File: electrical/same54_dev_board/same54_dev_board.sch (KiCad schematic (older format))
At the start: 8 parts

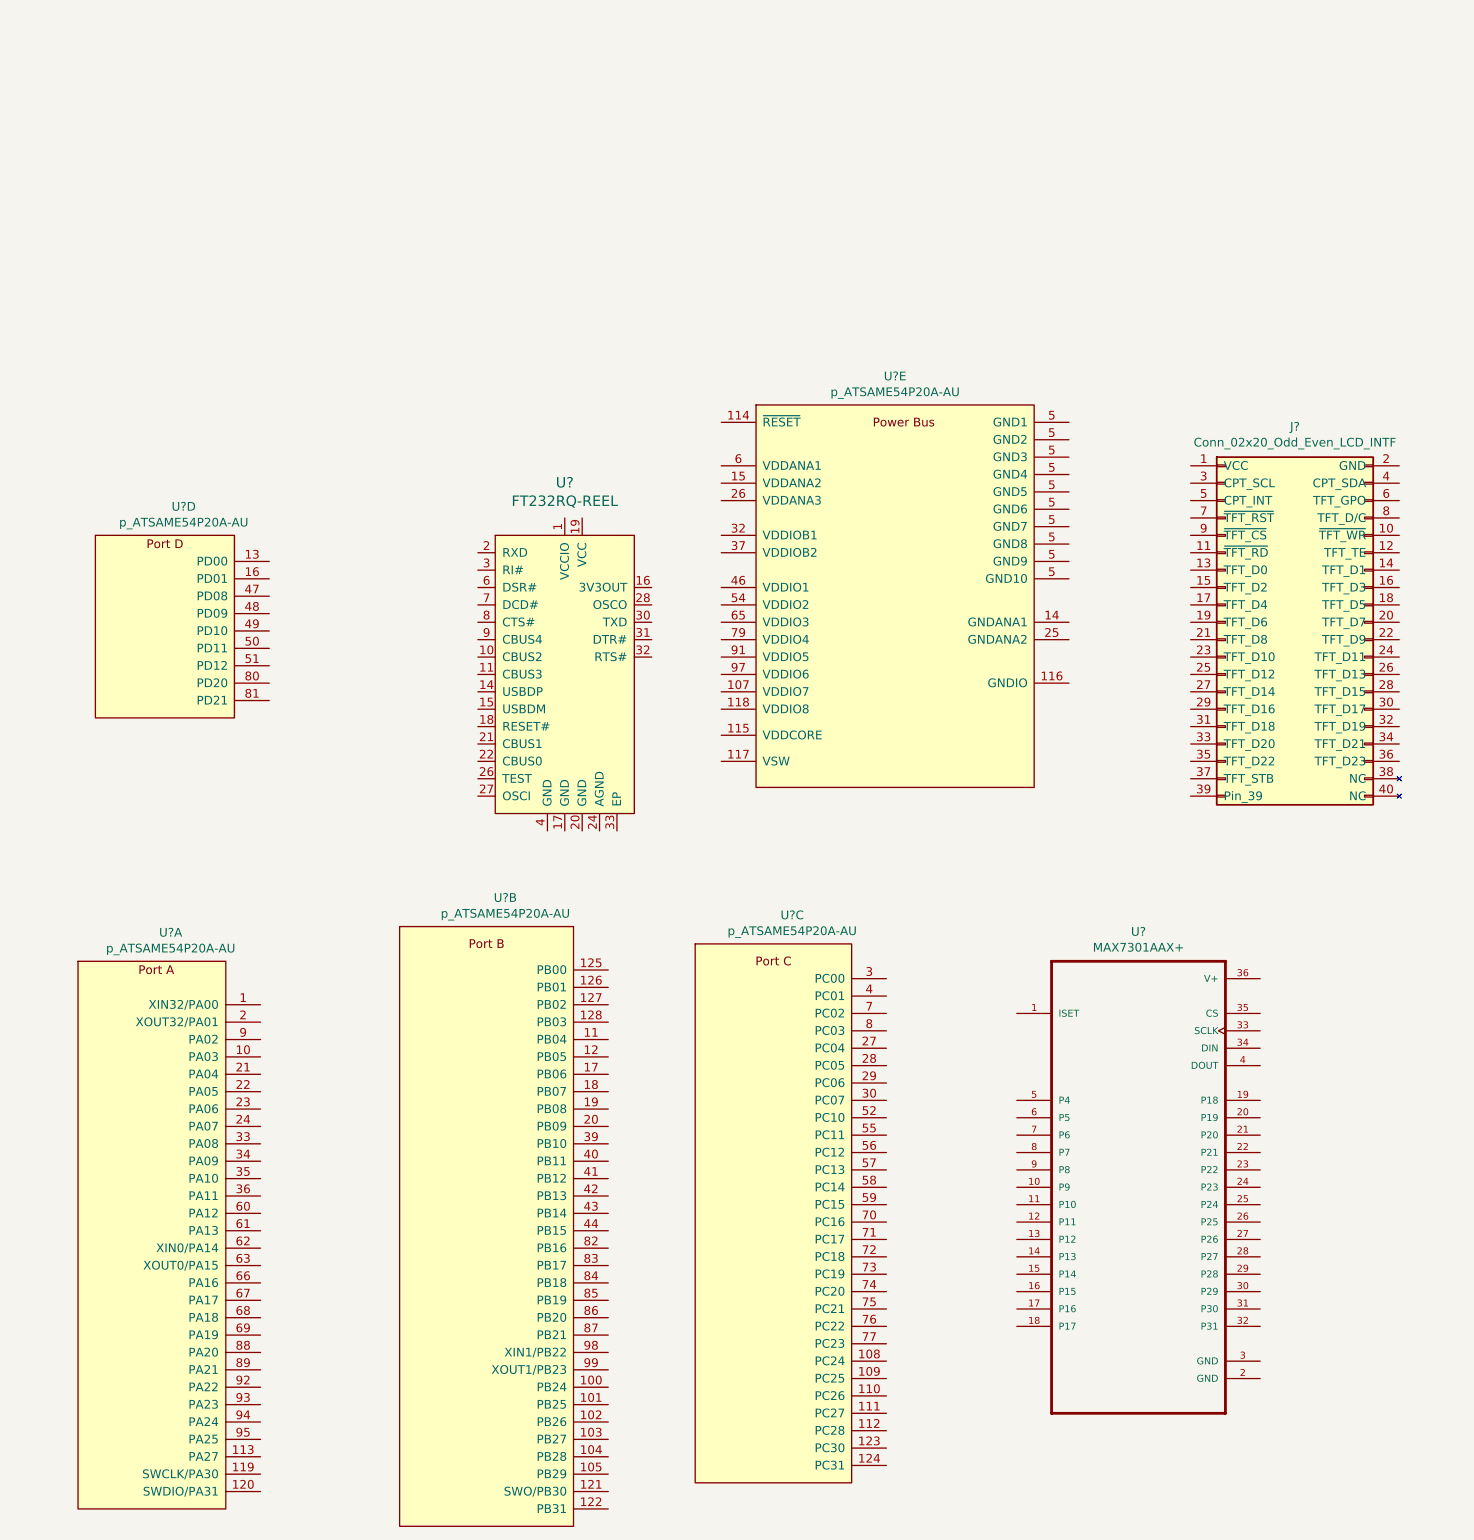
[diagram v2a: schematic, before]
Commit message: Added hierarchical pins for some components, finished io expander to lcd bus, going with 2x20 icd block header for the tft bus but dont have a part number for digikey
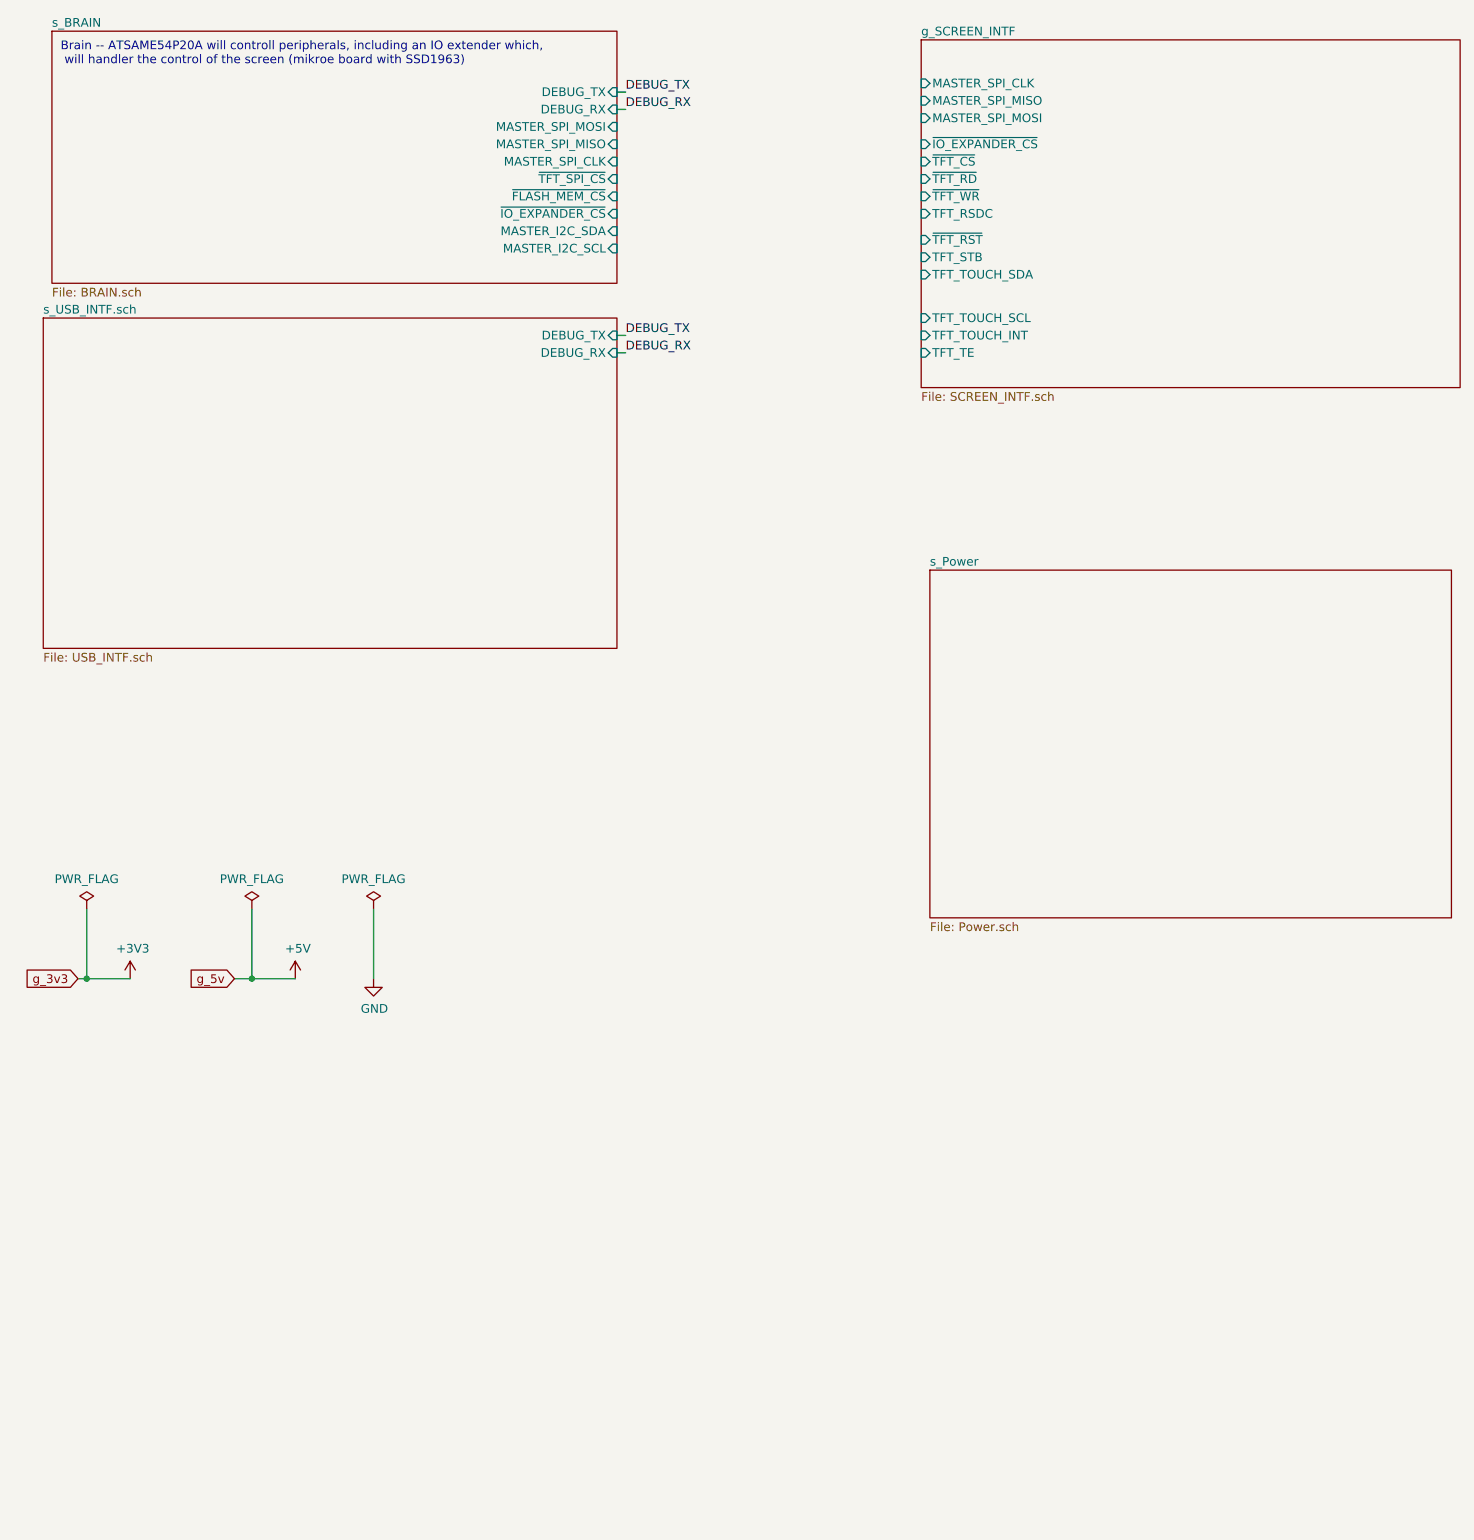
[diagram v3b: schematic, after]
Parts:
- removed J?: Conn_02x20_Odd_Even_LCD_INTF, symbol Conn_02x20_LCD_INTF:Conn_02x20_Odd_Even_LCD_INTF
- removed U?: FT232RQ-REEL, digikey-footprints:QFN-32-1EP_5x5mm, symbol dk_Interface-Controllers:FT232RQ-REEL
- removed U? (x5): p_ATSAME54P20A-AU, symbol p_ATSAME54P20A-AU:p_ATSAME54P20A-AU
- removed U?: MAX7301AAX+, SOP80P1030X264-36N, symbol MAX7301AAX_:MAX7301AAX+
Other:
- note added: "Brain -- ATSAME54P20A will controll peripherals, including an IO extender which,\n will handler the control of the screen (mikroe board with SSD1963)"
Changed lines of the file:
@@
 EELAYER 30 0
 EELAYER END
-$Descr USLedger 17000 11000
+$Descr A 11000 8500
 encoding utf-8
-Sheet 1 1
+Sheet 1 5
 Title "Project Oracle"
 Date "2020-03-16"
@@
 Comment4 ""
 $EndDescr
+$Sheet
+S 5800 3900 3000 2000
+U 5E7872D3
+F0 "s_Power" 50
+F1 "Power.sch" 50
+$EndSheet
+$Sheet
+S 700  2450 3300 1900
+U 5E7C0F59
+F0 "s_USB_INTF.sch" 50
+F1 "USB_INTF.sch" 50
+F2 "DEBUG_TX" I R 4000 2550 50
+F3 "DEBUG_RX" I R 4000 2650 50
+$EndSheet
+$Sheet
+S 750  800  3250 1450
+U 5E805E4F
+F0 "s_BRAIN" 50
+F1 "BRAIN.sch" 50
+F2 "DEBUG_TX" I R 4000 1150 50
+F3 "DEBUG_RX" I R 4000 1250 50
+F4 "MASTER_SPI_MOSI" I R 4000 1350 50
+F5 "MASTER_SPI_MISO" I R 4000 1450 50
+F6 "MASTER_SPI_CLK" I R 4000 1550 50
+F7 "~TFT_SPI_CS" I R 4000 1650 50
+F8 "~FLASH_MEM_CS" I R 4000 1750 50
+F9 "MASTER_I2C_SDA" I R 4000 1950 50
+F10 "MASTER_I2C_SCL" I R 4000 2050 50
+F11 "~IO_EXPANDER_CS" I R 4000 1850 50
+$EndSheet
+Text Notes 800  1000 0    50   ~ 0
+Brain -- ATSAME54P20A will controll peripherals, including an IO extender which,\n will handler the control of the screen (mikroe board with SSD1963)
+Text GLabel 900  6250 0    50   Input ~ 0
+g_3v3
+Text GLabel 1800 6250 0    50   Input ~ 0
+g_5v
+$Sheet
+S 5750 850  3100 2000
+U 5E8589A7
+F0 "g_SCREEN_INTF" 50
+F1 "SCREEN_INTF.sch" 50
+F2 "MASTER_SPI_CLK" I L 5750 1100 50
+F3 "MASTER_SPI_MISO" I L 5750 1200 50
+F4 "MASTER_SPI_MOSI" I L 5750 1300 50
+F5 "~IO_EXPANDER_CS" I L 5750 1450 50
+F6 "~TFT_CS" I L 5750 1550 50
+F7 "~TFT_RD" I L 5750 1650 50
+F8 "~TFT_WR" I L 5750 1750 50
+F9 "TFT_RSDC" I L 5750 1850 50
+F10 "~TFT_RST" I L 5750 2000 50
+F11 "TFT_STB" I L 5750 2100 50
+F12 "TFT_TOUCH_SDA" I L 5750 2200 50
+F13 "TFT_TOUCH_SCL" I L 5750 2450 50
+F14 "TFT_TOUCH_INT" I L 5750 2550 50
+F15 "TFT_TE" I L 5750 2650 50
+$EndSheet
+Wire Wire Line
+	900  6250 950  6250
 $Comp
-L dk_Interface-Controllers:FT232RQ-REEL U?
-U 1 1 5E77AB6E
-P 3900 3700
-F 0 "U?" H 3700 4003 60  0000 C CNN
-F 1 "FT232RQ-REEL" H 3700 3897 60  0000 C CNN
-F 2 "digikey-footprints:QFN-32-1EP_5x5mm" H 4100 3900 60  0001 L CNN
-F 3 "https://www.ftdichip.com/Support/Documents/DataSheets/ICs/DS_FT232R.pdf" H 4100 4000 60  0001 L CNN
-F 4 "768-1008-1-ND" H 4100 4100 60  0001 L CNN "Digi-Key_PN"
-F 5 "FT232RQ-REEL" H 4100 4200 60  0001 L CNN "MPN"
-F 6 "Integrated Circuits (ICs)" H 4100 4300 60  0001 L CNN "Category"
-F 7 "Interface - Controllers" H 4100 4400 60  0001 L CNN "Family"
-F 8 "https://www.ftdichip.com/Support/Documents/DataSheets/ICs/DS_FT232R.pdf" H 4100 4500 60  0001 L CNN "DK_Datasheet_Link"
-F 9 "/product-detail/en/ftdi-future-technology-devices-international-ltd/FT232RQ-REEL/768-1008-1-ND/1836403" H 4100 4600 60  0001 L CNN "DK_Detail_Page"
-F 10 "IC USB FS SERIAL UART 32-QFN" H 4100 4700 60  0001 L CNN "Description"
-F 11 "FTDI, Future Technology Devices International Ltd" H 4100 4800 60  0001 L CNN "Manufacturer"
-F 12 "Active" H 4100 4900 60  0001 L CNN "Status"
-	1    3900 3700
+L power:+3V3 #PWR0101
+U 1 1 5E97BC15
+P 1200 6250
+F 0 "#PWR0101" H 1200 6100 50  0001 C CNN
+F 1 "+3V3" H 1215 6423 50  0000 C CNN
+F 2 "" H 1200 6250 50  0001 C CNN
+F 3 "" H 1200 6250 50  0001 C CNN
+	1    1200 6250
 	1    0    0    -1
 $EndComp
 $Comp
-L p_ATSAME54P20A-AU:p_ATSAME54P20A-AU U?
-U 1 1 5E7D4D4E
-P 1350 7150
-F 0 "U?" H 1433 8315 50  0000 C CNN
-F 1 "p_ATSAME54P20A-AU" H 1433 8224 50  0000 C CNN
-F 2 "" H 150 8400 50  0001 C CNN
-F 3 "" H 150 8400 50  0001 C CNN
-	1    1350 7150
+L power:+5V #PWR0102
+U 1 1 5E97C21D
+P 2150 6250
+F 0 "#PWR0102" H 2150 6100 50  0001 C CNN
+F 1 "+5V" H 2165 6423 50  0000 C CNN
+F 2 "" H 2150 6250 50  0001 C CNN
+F 3 "" H 2150 6250 50  0001 C CNN
+	1    2150 6250
 	1    0    0    -1
 $EndComp
 $Comp
-L p_ATSAME54P20A-AU:p_ATSAME54P20A-AU U?
-U 2 1 5E7D76F8
-P 3250 6850
-F 0 "U?" H 3358 7915 50  0000 C CNN
-F 1 "p_ATSAME54P20A-AU" H 3358 7824 50  0000 C CNN
-F 2 "" H 2050 8100 50  0001 C CNN
-F 3 "" H 2050 8100 50  0001 C CNN
-	2    3250 6850
+L power:PWR_FLAG #FLG0101
+U 1 1 5E97C674
+P 950 5850
+F 0 "#FLG0101" H 950 5925 50  0001 C CNN
+F 1 "PWR_FLAG" H 950 6023 50  0000 C CNN
+F 2 "" H 950 5850 50  0001 C CNN
+F 3 "~" H 950 5850 50  0001 C CNN
+	1    950  5850
 	1    0    0    -1
 $EndComp
+Wire Wire Line
+	950  6250 950  5850
+Connection ~ 950  6250
+Wire Wire Line
+	950  6250 1200 6250
 $Comp
-L p_ATSAME54P20A-AU:p_ATSAME54P20A-AU U?
-U 3 1 5E7DA3E5
-P 4900 6900
-F 0 "U?" H 5008 7915 50  0000 C CNN
-F 1 "p_ATSAME54P20A-AU" H 5008 7824 50  0000 C CNN
-F 2 "" H 3700 8150 50  0001 C CNN
-F 3 "" H 3700 8150 50  0001 C CNN
-	3    4900 6900
+L power:GND #PWR0103
+U 1 1 5E97DBEE
+P 2600 6250
+F 0 "#PWR0103" H 2600 6000 50  0001 C CNN
+F 1 "GND" H 2605 6077 50  0000 C CNN
+F 2 "" H 2600 6250 50  0001 C CNN
+F 3 "" H 2600 6250 50  0001 C CNN
+	1    2600 6250
 	1    0    0    -1
 $EndComp
+Wire Wire Line
+	1800 6250 1900 6250
 $Comp
-L p_ATSAME54P20A-AU:p_ATSAME54P20A-AU U?
-U 4 1 5E7DD1DD
-P 1400 4600
-F 0 "U?" H 1508 5665 50  0000 C CNN
-F 1 "p_ATSAME54P20A-AU" H 1508 5574 50  0000 C CNN
-F 2 "" H 200 5850 50  0001 C CNN
-F 3 "" H 200 5850 50  0001 C CNN
-	4    1400 4600
+L power:PWR_FLAG #FLG0102
+U 1 1 5E97F87F
+P 1900 5850
+F 0 "#FLG0102" H 1900 5925 50  0001 C CNN
+F 1 "PWR_FLAG" H 1900 6023 50  0000 C CNN
+F 2 "" H 1900 5850 50  0001 C CNN
+F 3 "~" H 1900 5850 50  0001 C CNN
+	1    1900 5850
 	1    0    0    -1
 $EndComp
+Wire Wire Line
+	1900 6250 1900 5850
+Connection ~ 1900 6250
+Wire Wire Line
+	1900 6250 2150 6250
 $Comp
-L p_ATSAME54P20A-AU:p_ATSAME54P20A-AU U?
-U 5 1 5E7E22D4
-P 5600 3700
-F 0 "U?" H 5600 4615 50  0000 C CNN
-F 1 "p_ATSAME54P20A-AU" H 5600 4524 50  0000 C CNN
-F 2 "" H 4400 4950 50  0001 C CNN
-F 3 "" H 4400 4950 50  0001 C CNN
-	5    5600 3700
+L power:PWR_FLAG #FLG0103
+U 1 1 5E980A5B
+P 2600 5850
+F 0 "#FLG0103" H 2600 5925 50  0001 C CNN
+F 1 "PWR_FLAG" H 2600 6023 50  0000 C CNN
+F 2 "" H 2600 5850 50  0001 C CNN
+F 3 "~" H 2600 5850 50  0001 C CNN
+	1    2600 5850
 	1    0    0    -1
 $EndComp
-$Comp
-L Conn_02x20_LCD_INTF:Conn_02x20_Odd_Even_LCD_INTF J?
-U 1 1 5E896181
-P 7900 4200
-F 0 "J?" H 7900 5325 50  0000 C CNN
-F 1 "Conn_02x20_Odd_Even_LCD_INTF" H 7900 5234 50  0000 C CNN
-F 2 "" H 7500 4200 50  0001 C CNN
-F 3 "~" H 7500 4200 50  0001 C CNN
-	1    7900 4200
-	1    0    0    -1
-$EndComp
-$Comp
-L MAX7301AAX_:MAX7301AAX+ U?
-U 1 1 5E8C31CA
-P 7000 7450
-F 0 "U?" H 7000 8920 50  0000 C CNN
-F 1 "MAX7301AAX+" H 7000 8829 50  0000 C CNN
-F 2 "SOP80P1030X264-36N" H 7000 7450 50  0001 L BNN
-F 3 "Maxim Integrated" H 7000 7450 50  0001 L BNN
-F 4 "None" H 7000 7450 50  0001 L BNN "Field4"
-F 5 "Interface IC - I/O extensions Maxim Integrated MAX7301AAX+ SPI 26 MHz SSOP 36" H 7000 7450 50  0001 L BNN "Field5"
-F 6 "SSOP-36 Maxim" H 7000 7450 50  0001 L BNN "Field6"
-F 7 "Unavailable" H 7000 7450 50  0001 L BNN "Field7"
-F 8 "MAX7301AAX+" H 7000 7450 50  0001 L BNN "Field8"
-	1    7000 7450
-	1    0    0    -1
-$EndComp
+Wire Wire Line
+	2600 6250 2600 5850
+Text Label 4050 1150 0    50   ~ 0
+DEBUG_TX
+Wire Wire Line
+	4000 1150 4050 1150
+Text Label 4050 2550 0    50   ~ 0
+DEBUG_TX
+Wire Wire Line
+	4000 1250 4050 1250
+Text Label 4050 1250 0    50   ~ 0
+DEBUG_RX
+Wire Wire Line
+	4000 2550 4050 2550
+Wire Wire Line
+	4000 2650 4050 2650
+Text Label 4050 2650 0    50   ~ 0
+DEBUG_RX
 $EndSCHEMATC

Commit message: Trying to figure out how I want to do power...
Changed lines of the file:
@@
 S 5750 850  3100 2000
 U 5E8589A7
-F0 "g_SCREEN_INTF" 50
+F0 "s_SCREEN_INTF" 50
 F1 "SCREEN_INTF.sch" 50
 F2 "MASTER_SPI_CLK" I L 5750 1100 50

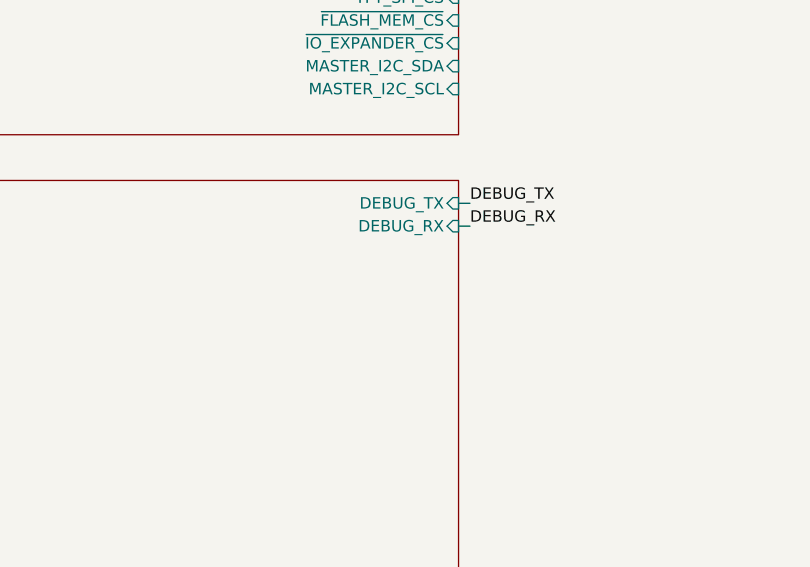
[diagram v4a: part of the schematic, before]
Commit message: going with barrel jack 5v+2A optional input, with usb supplying 400mA + 100mA for internals
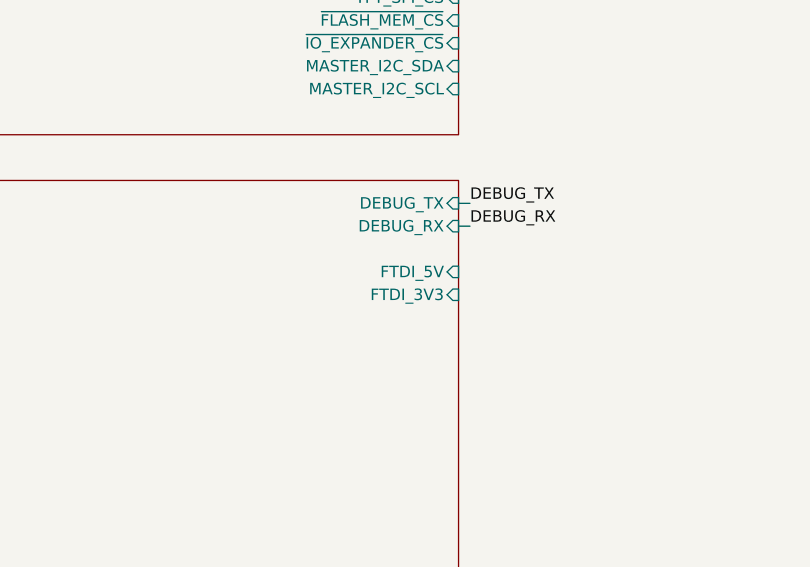
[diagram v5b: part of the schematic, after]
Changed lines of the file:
@@
 F2 "DEBUG_TX" I R 4000 2550 50
 F3 "DEBUG_RX" I R 4000 2650 50
+F4 "FTDI_5V" I R 4000 2850 50
+F5 "FTDI_3V3" I R 4000 2950 50
 $EndSheet
 $Sheet
